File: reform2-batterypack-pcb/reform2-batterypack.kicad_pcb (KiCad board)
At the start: 2 copper layers, 91 x 66 mm, 14 parts, among them J1 Conn_01x05_Female, U1 KEYSTONE_54, U2 KEYSTONE_54, U3 KEYSTONE_54, U4 KEYSTONE_54

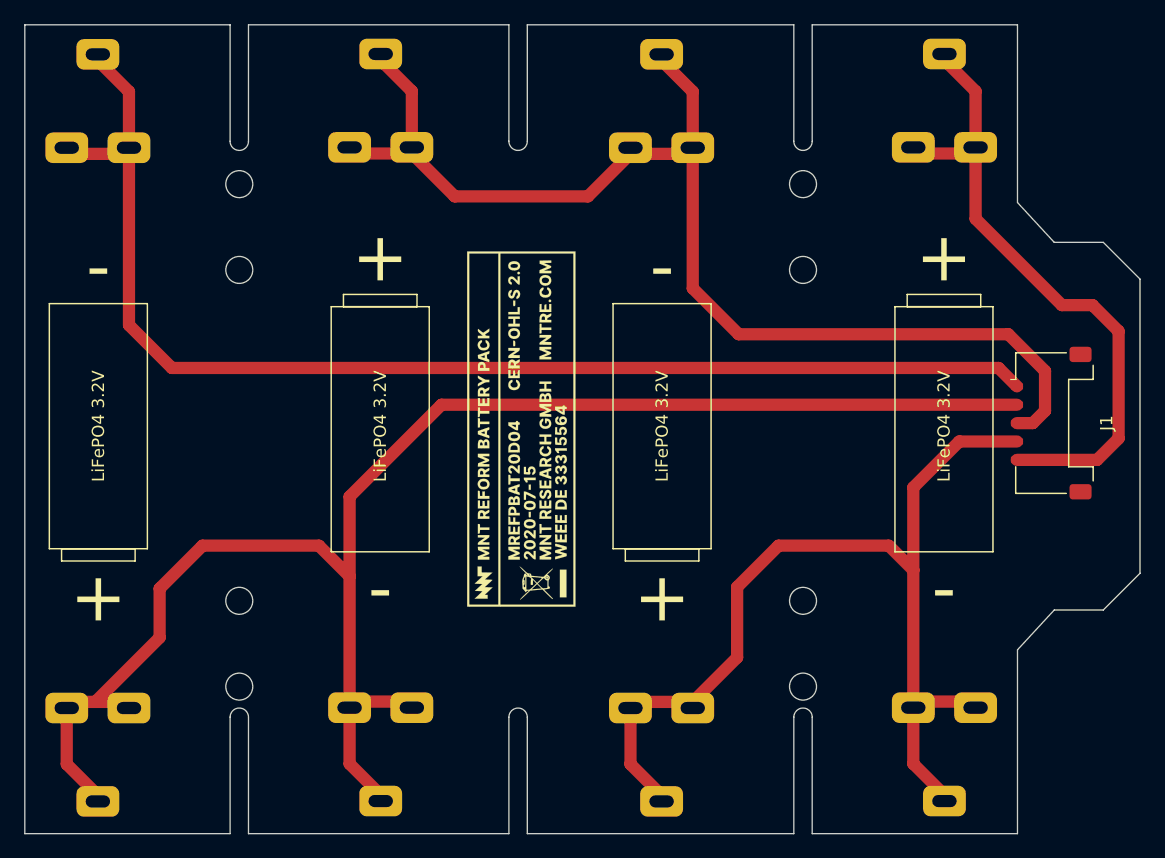
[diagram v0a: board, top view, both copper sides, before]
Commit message: reform2: update PCBs incl. badges to production revs, add keyboard lettering, misc docs
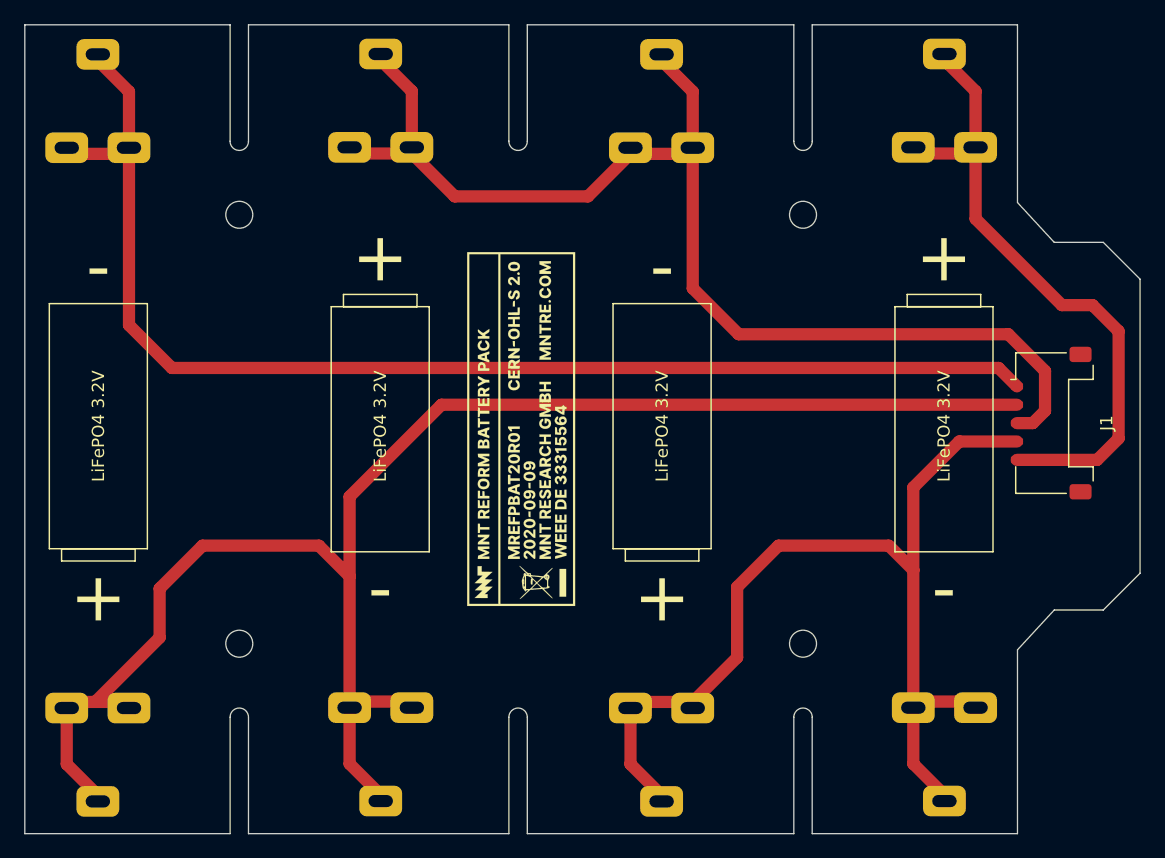
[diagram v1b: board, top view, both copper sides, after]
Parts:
- removed H1, H2, H3, H4: MountingHole, MountingHole:MountingHole_2.2mm_M2
- moved H5 4.50 mm to (113.0, 103.0)
- moved H6 4.50 mm to (159.0, 103.0)
- moved H7 3.50 mm to (113.0, 138.0)
- moved H8 3.50 mm to (159.0, 138.0)
